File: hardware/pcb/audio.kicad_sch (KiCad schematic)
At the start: 10 parts, among them IC3 TAC5212, J6 PJ-342, J7 PJ-242

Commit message: mainboard: reannotated schematic
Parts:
- renumbered C41 to C111, C47 to C112, C45 to C113, C46 to C114, J6 to J4, J7 to J5, R28 to R32, R26 to R33, R27 to R34
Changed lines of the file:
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@@
 		(in_pos_files yes)
 		(dnp no)
-		(property "Reference" "#PWR087"
+		(property "Reference" "#PWR0104"
 			(at 58.42 33.02 0)
 			(hide yes)
@@
 			(project "meko"
 				(path "/da54f10a-146b-4941-a9c7-55c7173bb101/073f6085-34ed-486a-9dc9-0ac1ede2fab6"
-					(reference "#PWR087")
+					(reference "#PWR0104")
 					(unit 1)
 				)
@@
 		(in_pos_files yes)
 		(dnp no)
-		(property "Reference" "C45"
+		(property "Reference" "C113"
 			(at 52.578 29.464 90)
 			(show_name no)
@@
 			(project "meko"
 				(path "/da54f10a-146b-4941-a9c7-55c7173bb101/073f6085-34ed-486a-9dc9-0ac1ede2fab6"
-					(reference "C45")
+					(reference "C113")
 					(unit 1)
 				)
@@
 		(in_pos_files yes)
 		(dnp no)
-		(property "Reference" "C41"
+		(property "Reference" "C111"
 			(at 62.738 20.574 90)
 			(show_name no)
@@
 			(project "meko"
 				(path "/da54f10a-146b-4941-a9c7-55c7173bb101/073f6085-34ed-486a-9dc9-0ac1ede2fab6"
-					(reference "C41")
+					(reference "C111")
 					(unit 1)
 				)
@@
 		(dnp no)
 		(fields_autoplaced yes)
-		(property "Reference" "#PWR095"
+		(property "Reference" "#PWR0111"
 			(at 44.45 82.55 0)
 			(hide yes)
@@
 			(project "meko"
 				(path "/da54f10a-146b-4941-a9c7-55c7173bb101/073f6085-34ed-486a-9dc9-0ac1ede2fab6"
-					(reference "#PWR095")
+					(reference "#PWR0111")
 					(unit 1)
 				)
@@
 		(in_pos_files yes)
 		(dnp no)
-		(property "Reference" "#PWR0119"
+		(property "Reference" "#PWR0108"
 			(at 97.79 38.1 0)
 			(hide yes)
@@
 			(project "meko"
 				(path "/da54f10a-146b-4941-a9c7-55c7173bb101/073f6085-34ed-486a-9dc9-0ac1ede2fab6"
-					(reference "#PWR0119")
+					(reference "#PWR0108")
 					(unit 1)
 				)
@@
 		(in_pos_files yes)
 		(dnp no)
-		(property "Reference" "R27"
+		(property "Reference" "R34"
 			(at 151.638 93.218 0)
 			(show_name no)
@@
 			(project "meko"
 				(path "/da54f10a-146b-4941-a9c7-55c7173bb101/073f6085-34ed-486a-9dc9-0ac1ede2fab6"
-					(reference "R27")
+					(reference "R34")
 					(unit 1)
 				)
@@
 		(in_pos_files yes)
 		(dnp no)
-		(property "Reference" "#PWR094"
+		(property "Reference" "#PWR0105"
 			(at 88.9 33.02 0)
 			(hide yes)
@@
 			(project "meko"
 				(path "/da54f10a-146b-4941-a9c7-55c7173bb101/073f6085-34ed-486a-9dc9-0ac1ede2fab6"
-					(reference "#PWR094")
+					(reference "#PWR0105")
 					(unit 1)
 				)
@@
 		(in_pos_files yes)
 		(dnp no)
-		(property "Reference" "R26"
+		(property "Reference" "R33"
 			(at 151.638 65.278 0)
 			(show_name no)
@@
 			(project "meko"
 				(path "/da54f10a-146b-4941-a9c7-55c7173bb101/073f6085-34ed-486a-9dc9-0ac1ede2fab6"
-					(reference "R26")
+					(reference "R33")
 					(unit 1)
 				)
@@
 		(in_pos_files yes)
 		(dnp no)
-		(property "Reference" "#PWR0118"
+		(property "Reference" "#PWR0107"
 			(at 49.53 38.1 0)
 			(hide yes)
@@
 			(project "meko"
 				(path "/da54f10a-146b-4941-a9c7-55c7173bb101/073f6085-34ed-486a-9dc9-0ac1ede2fab6"
-					(reference "#PWR0118")
+					(reference "#PWR0107")
 					(unit 1)
 				)
@@
 		(in_pos_files yes)
 		(dnp no)
-		(property "Reference" "#PWR098"
+		(property "Reference" "#PWR0110"
 			(at 154.94 76.2 0)
 			(hide yes)
@@
 			(project "meko"
 				(path "/da54f10a-146b-4941-a9c7-55c7173bb101/073f6085-34ed-486a-9dc9-0ac1ede2fab6"
-					(reference "#PWR098")
+					(reference "#PWR0110")
 					(unit 1)
 				)
@@
 		(in_pos_files yes)
 		(dnp no)
-		(property "Reference" "#PWR090"
+		(property "Reference" "#PWR0103"
 			(at 53.34 21.59 0)
 			(hide yes)
@@
 			(project "meko"
 				(path "/da54f10a-146b-4941-a9c7-55c7173bb101/073f6085-34ed-486a-9dc9-0ac1ede2fab6"
-					(reference "#PWR090")
+					(reference "#PWR0103")
 					(unit 1)
 				)
@@
 		(in_pos_files yes)
 		(dnp no)
-		(property "Reference" "#PWR089"
+		(property "Reference" "#PWR0106"
 			(at 72.39 36.83 0)
 			(hide yes)
@@
 			(project "meko"
 				(path "/da54f10a-146b-4941-a9c7-55c7173bb101/073f6085-34ed-486a-9dc9-0ac1ede2fab6"
-					(reference "#PWR089")
+					(reference "#PWR0106")
 					(unit 1)
 				)
@@
 		(in_pos_files yes)
 		(dnp no)
-		(property "Reference" "C47"
+		(property "Reference" "C112"
 			(at 75.438 28.194 90)
 			(show_name no)
@@
 			(project "meko"
 				(path "/da54f10a-146b-4941-a9c7-55c7173bb101/073f6085-34ed-486a-9dc9-0ac1ede2fab6"
-					(reference "C47")
+					(reference "C112")
 					(unit 1)
 				)
@@
 		(dnp no)
 		(fields_autoplaced yes)
-		(property "Reference" "J7"
+		(property "Reference" "J5"
 			(at 171.45 83.1849 0)
 			(show_name no)
@@
 			(project "meko"
 				(path "/da54f10a-146b-4941-a9c7-55c7173bb101/073f6085-34ed-486a-9dc9-0ac1ede2fab6"
-					(reference "J7")
+					(reference "J5")
 					(unit 1)
 				)
@@
 		(dnp no)
 		(fields_autoplaced yes)
-		(property "Reference" "J6"
+		(property "Reference" "J4"
 			(at 171.45 55.2449 0)
 			(show_name no)
@@
 			(project "meko"
 				(path "/da54f10a-146b-4941-a9c7-55c7173bb101/073f6085-34ed-486a-9dc9-0ac1ede2fab6"
-					(reference "J6")
+					(reference "J4")
 					(unit 1)
 				)
@@
 		(in_pos_files yes)
 		(dnp no)
-		(property "Reference" "#PWR0100"
+		(property "Reference" "#PWR0109"
 			(at 109.22 46.99 0)
 			(hide yes)
@@
 			(project "meko"
 				(path "/da54f10a-146b-4941-a9c7-55c7173bb101/073f6085-34ed-486a-9dc9-0ac1ede2fab6"
-					(reference "#PWR0100")
+					(reference "#PWR0109")
 					(unit 1)
 				)
@@
 		(in_pos_files yes)
 		(dnp no)
-		(property "Reference" "C46"
+		(property "Reference" "C114"
 			(at 94.742 29.464 90)
 			(show_name no)
@@
 			(project "meko"
 				(path "/da54f10a-146b-4941-a9c7-55c7173bb101/073f6085-34ed-486a-9dc9-0ac1ede2fab6"
-					(reference "C46")
+					(reference "C114")
 					(unit 1)
 				)
@@
 		(dnp no)
 		(fields_autoplaced yes)
-		(property "Reference" "#PWR086"
+		(property "Reference" "#PWR0112"
 			(at 73.66 90.17 0)
 			(hide yes)
@@
 			(project "meko"
 				(path "/da54f10a-146b-4941-a9c7-55c7173bb101/073f6085-34ed-486a-9dc9-0ac1ede2fab6"
-					(reference "#PWR086")
+					(reference "#PWR0112")
 					(unit 1)
 				)
@@
 		(in_pos_files yes)
 		(dnp no)
-		(property "Reference" "R28"
+		(property "Reference" "R32"
 			(at 117.602 46.228 0)
 			(show_name no)
@@
 			(project "meko"
 				(path "/da54f10a-146b-4941-a9c7-55c7173bb101/073f6085-34ed-486a-9dc9-0ac1ede2fab6"
-					(reference "R28")
+					(reference "R32")
 					(unit 1)
 				)
@@
 		(in_pos_files yes)
 		(dnp no)
-		(property "Reference" "#PWR099"
+		(property "Reference" "#PWR0113"
 			(at 154.94 104.14 0)
 			(hide yes)
@@
 			(project "meko"
 				(path "/da54f10a-146b-4941-a9c7-55c7173bb101/073f6085-34ed-486a-9dc9-0ac1ede2fab6"
-					(reference "#PWR099")
-					(unit 1)
-				)
+					(reference "#PWR0113")
+					(unit 1)
+				)

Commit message: added a bunch testpoints
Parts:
- added TP52: AU_BCLK, TestPoint:TestPoint_Pad_D1.0mm, symbol Connector:TestPoint
- added TP53: AU_FSYNC, TestPoint:TestPoint_Pad_D1.0mm, symbol Connector:TestPoint
- added TP54: AU_DOUT, TestPoint:TestPoint_Pad_D1.0mm, symbol Connector:TestPoint
- added TP55: AU_DIN, TestPoint:TestPoint_Pad_D1.0mm, symbol Connector:TestPoint
- added TP56: AU_GPIO1, TestPoint:TestPoint_Pad_D1.0mm, symbol Connector:TestPoint
- added TP57: AU_GPIO2, TestPoint:TestPoint_Pad_D1.0mm, symbol Connector:TestPoint
- added TP58: AU_GPO1, TestPoint:TestPoint_Pad_D1.0mm, symbol Connector:TestPoint
- added TP59: AU_GPI1, TestPoint:TestPoint_Pad_D1.0mm, symbol Connector:TestPoint
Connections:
- net BCLK: now also TP52.1
- net DIN: now also TP55.1
- net DOUT: now also TP54.1
- net FSYNC: now also TP53.1
- net GPI1: now also TP59.1
- net GPIO1: now also TP56.1
- net GPIO2: now also TP57.1
- net GPO1: now also TP58.1

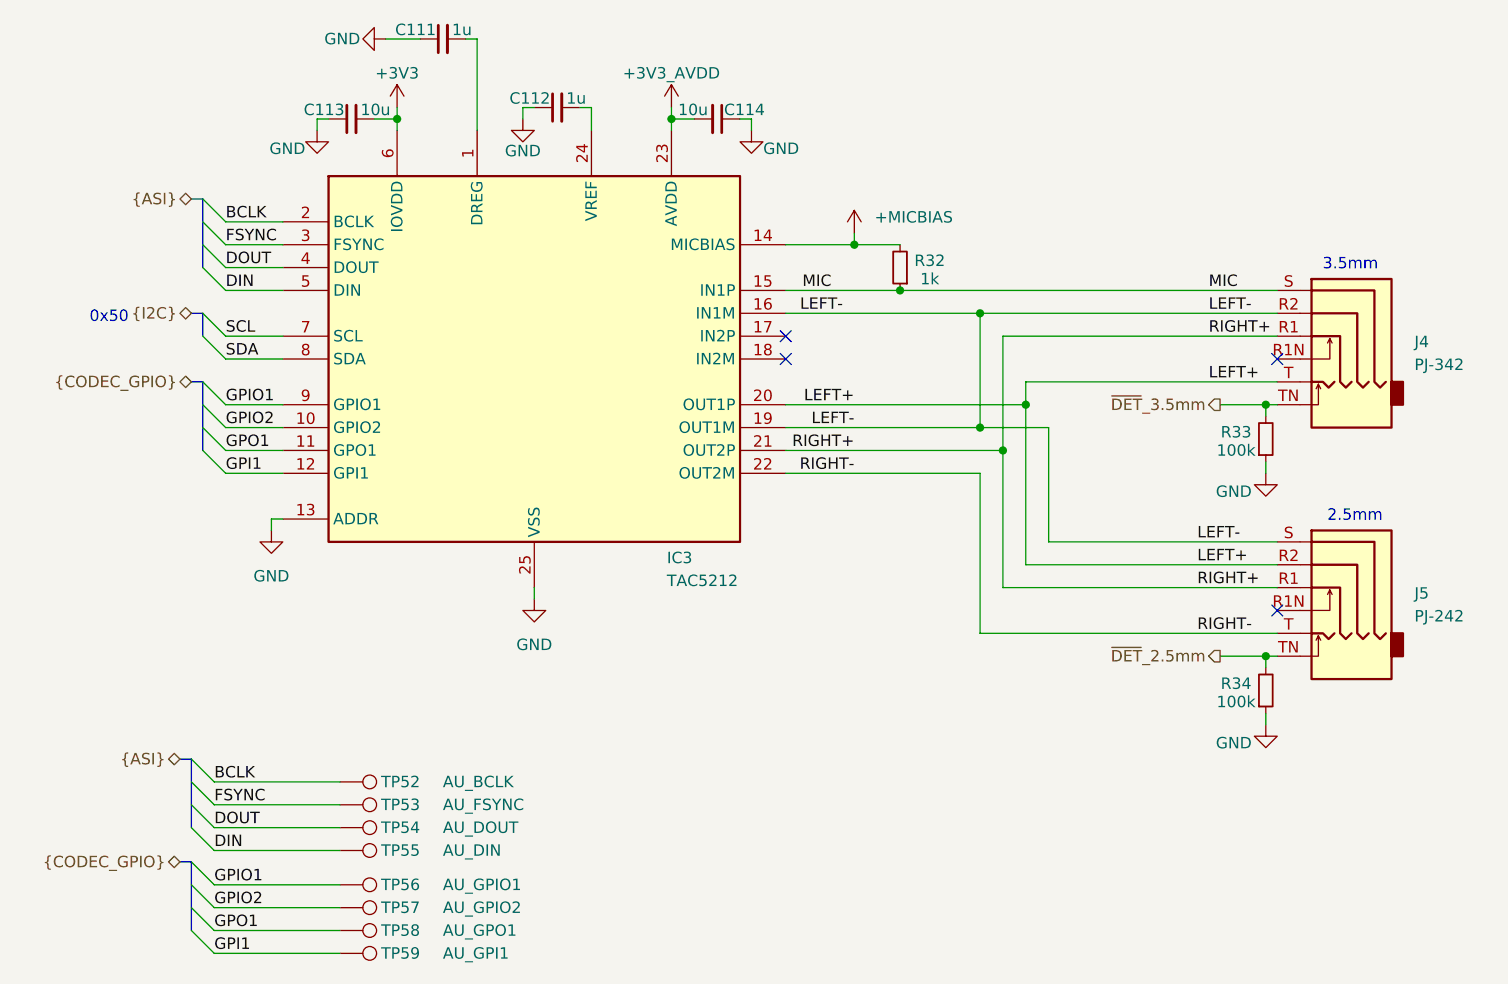
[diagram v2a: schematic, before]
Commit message: removed testpoints on sd cards, since I can probe the pins there
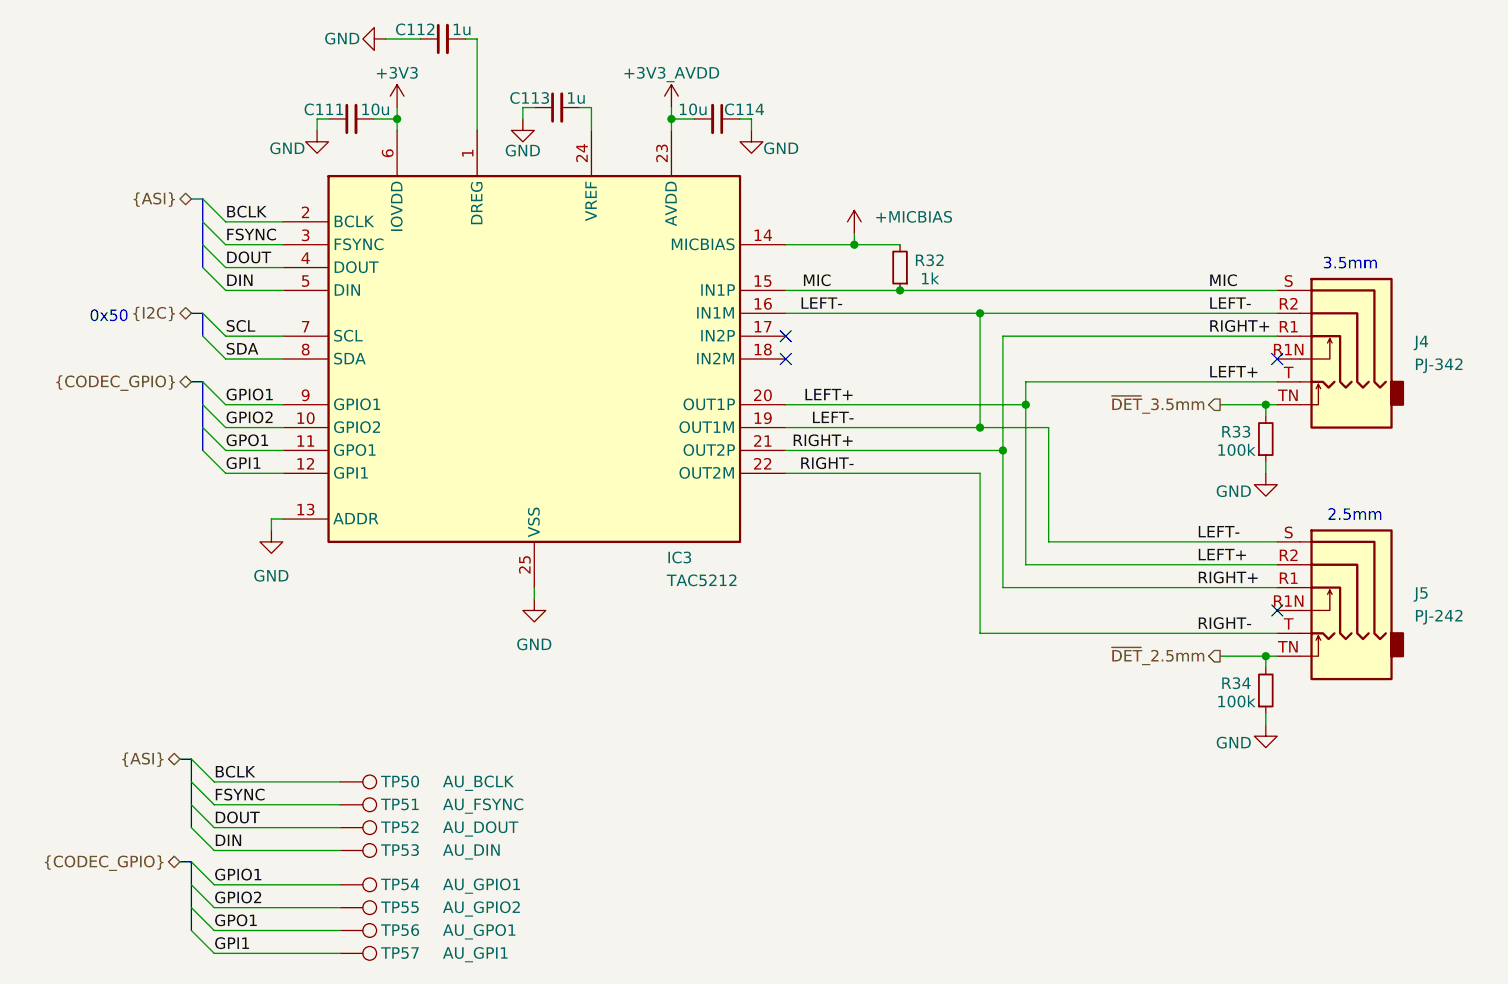
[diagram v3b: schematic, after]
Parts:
- renumbered C113 to C111, C111 to C112, C112 to C113, TP52 to TP50, TP53 to TP51, TP54 to TP52, TP55 to TP53, TP56 to TP54, TP57 to TP55, TP58 to TP56, TP59 to TP57
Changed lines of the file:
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@@
 		(in_pos_files yes)
 		(dnp no)
-		(property "Reference" "#PWR0104"
+		(property "Reference" "#PWR0106"
 			(at 58.42 33.02 0)
 			(hide yes)
@@
 			(project "meko"
 				(path "/da54f10a-146b-4941-a9c7-55c7173bb101/073f6085-34ed-486a-9dc9-0ac1ede2fab6"
-					(reference "#PWR0104")
+					(reference "#PWR0106")
 					(unit 1)
 				)
@@
 		(in_pos_files yes)
 		(dnp no)
-		(property "Reference" "C113"
+		(property "Reference" "C111"
 			(at 52.578 29.464 90)
 			(show_name no)
@@
 			(project "meko"
 				(path "/da54f10a-146b-4941-a9c7-55c7173bb101/073f6085-34ed-486a-9dc9-0ac1ede2fab6"
-					(reference "C113")
+					(reference "C111")
 					(unit 1)
 				)
@@
 		(in_pos_files yes)
 		(dnp no)
-		(property "Reference" "C111"
+		(property "Reference" "C112"
 			(at 62.738 20.574 90)
 			(show_name no)
@@
 			(project "meko"
 				(path "/da54f10a-146b-4941-a9c7-55c7173bb101/073f6085-34ed-486a-9dc9-0ac1ede2fab6"
-					(reference "C111")
+					(reference "C112")
 					(unit 1)
 				)
@@
 		(in_pos_files yes)
 		(dnp no)
-		(property "Reference" "TP52"
+		(property "Reference" "TP50"
 			(at 56.642 104.14 90)
 			(show_name no)
@@
 			(project "meko"
 				(path "/da54f10a-146b-4941-a9c7-55c7173bb101/073f6085-34ed-486a-9dc9-0ac1ede2fab6"
-					(reference "TP52")
+					(reference "TP50")
 					(unit 1)
 				)
@@
 		(in_pos_files yes)
 		(dnp no)
-		(property "Reference" "TP56"
+		(property "Reference" "TP54"
 			(at 56.642 115.57 90)
 			(show_name no)
@@
 			(project "meko"
 				(path "/da54f10a-146b-4941-a9c7-55c7173bb101/073f6085-34ed-486a-9dc9-0ac1ede2fab6"
-					(reference "TP56")
+					(reference "TP54")
 					(unit 1)
 				)
@@
 		(dnp no)
 		(fields_autoplaced yes)
-		(property "Reference" "#PWR0111"
+		(property "Reference" "#PWR0103"
 			(at 44.45 82.55 0)
 			(hide yes)
@@
 			(project "meko"
 				(path "/da54f10a-146b-4941-a9c7-55c7173bb101/073f6085-34ed-486a-9dc9-0ac1ede2fab6"
-					(reference "#PWR0111")
+					(reference "#PWR0103")
 					(unit 1)
 				)
@@
 		(in_pos_files yes)
 		(dnp no)
-		(property "Reference" "TP54"
+		(property "Reference" "TP52"
 			(at 56.642 109.22 90)
 			(show_name no)
@@
 			(project "meko"
 				(path "/da54f10a-146b-4941-a9c7-55c7173bb101/073f6085-34ed-486a-9dc9-0ac1ede2fab6"
-					(reference "TP54")
+					(reference "TP52")
 					(unit 1)
 				)
@@
 		(in_pos_files yes)
 		(dnp no)
-		(property "Reference" "#PWR0108"
+		(property "Reference" "#PWR0110"
 			(at 97.79 38.1 0)
 			(hide yes)
@@
 			(project "meko"
 				(path "/da54f10a-146b-4941-a9c7-55c7173bb101/073f6085-34ed-486a-9dc9-0ac1ede2fab6"
-					(reference "#PWR0108")
+					(reference "#PWR0110")
 					(unit 1)
 				)
@@
 		(in_pos_files yes)
 		(dnp no)
-		(property "Reference" "TP53"
+		(property "Reference" "TP51"
 			(at 56.642 106.68 90)
 			(show_name no)
@@
 			(project "meko"
 				(path "/da54f10a-146b-4941-a9c7-55c7173bb101/073f6085-34ed-486a-9dc9-0ac1ede2fab6"
-					(reference "TP53")
+					(reference "TP51")
 					(unit 1)
 				)
@@
 		(in_pos_files yes)
 		(dnp no)
-		(property "Reference" "TP57"
+		(property "Reference" "TP55"
 			(at 56.642 118.11 90)
 			(show_name no)
@@
 			(project "meko"
 				(path "/da54f10a-146b-4941-a9c7-55c7173bb101/073f6085-34ed-486a-9dc9-0ac1ede2fab6"
-					(reference "TP57")
+					(reference "TP55")
 					(unit 1)
 				)
@@
 		(in_pos_files yes)
 		(dnp no)
-		(property "Reference" "#PWR0105"
+		(property "Reference" "#PWR0109"
 			(at 88.9 33.02 0)
 			(hide yes)
@@
 			(project "meko"
 				(path "/da54f10a-146b-4941-a9c7-55c7173bb101/073f6085-34ed-486a-9dc9-0ac1ede2fab6"
-					(reference "#PWR0105")
+					(reference "#PWR0109")
 					(unit 1)
 				)
@@
 		(in_pos_files yes)
 		(dnp no)
-		(property "Reference" "#PWR0107"
+		(property "Reference" "#PWR0104"
 			(at 49.53 38.1 0)
 			(hide yes)
@@
 			(project "meko"
 				(path "/da54f10a-146b-4941-a9c7-55c7173bb101/073f6085-34ed-486a-9dc9-0ac1ede2fab6"
-					(reference "#PWR0107")
+					(reference "#PWR0104")
 					(unit 1)
 				)
@@
 		(in_pos_files yes)
 		(dnp no)
-		(property "Reference" "#PWR0110"
+		(property "Reference" "#PWR0112"
 			(at 154.94 76.2 0)
 			(hide yes)
@@
 			(project "meko"
 				(path "/da54f10a-146b-4941-a9c7-55c7173bb101/073f6085-34ed-486a-9dc9-0ac1ede2fab6"
-					(reference "#PWR0110")
+					(reference "#PWR0112")
 					(unit 1)
 				)
@@
 		(in_pos_files yes)
 		(dnp no)
-		(property "Reference" "TP59"
+		(property "Reference" "TP57"
 			(at 56.642 123.19 90)
 			(show_name no)
@@
 			(project "meko"
 				(path "/da54f10a-146b-4941-a9c7-55c7173bb101/073f6085-34ed-486a-9dc9-0ac1ede2fab6"
-					(reference "TP59")
+					(reference "TP57")
 					(unit 1)
 				)
@@
 		(in_pos_files yes)
 		(dnp no)
-		(property "Reference" "#PWR0103"
+		(property "Reference" "#PWR0105"
 			(at 50.8 21.59 0)
 			(hide yes)
@@
 			(project "meko"
 				(path "/da54f10a-146b-4941-a9c7-55c7173bb101/073f6085-34ed-486a-9dc9-0ac1ede2fab6"
-					(reference "#PWR0103")
+					(reference "#PWR0105")
 					(unit 1)
 				)
@@
 		(in_pos_files yes)
 		(dnp no)
-		(property "Reference" "#PWR0106"
+		(property "Reference" "#PWR0107"
 			(at 72.39 36.83 0)
 			(hide yes)
@@
 			(project "meko"
 				(path "/da54f10a-146b-4941-a9c7-55c7173bb101/073f6085-34ed-486a-9dc9-0ac1ede2fab6"
-					(reference "#PWR0106")
+					(reference "#PWR0107")
 					(unit 1)
 				)
@@
 		(in_pos_files yes)
 		(dnp no)
-		(property "Reference" "C112"
+		(property "Reference" "C113"
 			(at 75.438 28.194 90)
 			(show_name no)
@@
 			(project "meko"
 				(path "/da54f10a-146b-4941-a9c7-55c7173bb101/073f6085-34ed-486a-9dc9-0ac1ede2fab6"
-					(reference "C112")
+					(reference "C113")
 					(unit 1)
 				)
@@
 		(in_pos_files yes)
 		(dnp no)
-		(property "Reference" "TP55"
+		(property "Reference" "TP53"
 			(at 56.642 111.76 90)
 			(show_name no)
@@
 			(project "meko"
 				(path "/da54f10a-146b-4941-a9c7-55c7173bb101/073f6085-34ed-486a-9dc9-0ac1ede2fab6"
-					(reference "TP55")
+					(reference "TP53")
 					(unit 1)
 				)
@@
 		(in_pos_files yes)
 		(dnp no)
-		(property "Reference" "#PWR0109"
+		(property "Reference" "#PWR0111"
 			(at 109.22 46.99 0)
 			(hide yes)
@@
 			(project "meko"
 				(path "/da54f10a-146b-4941-a9c7-55c7173bb101/073f6085-34ed-486a-9dc9-0ac1ede2fab6"
-					(reference "#PWR0109")
+					(reference "#PWR0111")
 					(unit 1)
 				)
@@
 		(dnp no)
 		(fields_autoplaced yes)
-		(property "Reference" "#PWR0112"
+		(property "Reference" "#PWR0108"
 			(at 73.66 90.17 0)
 			(hide yes)
@@
 			(project "meko"
 				(path "/da54f10a-146b-4941-a9c7-55c7173bb101/073f6085-34ed-486a-9dc9-0ac1ede2fab6"
-					(reference "#PWR0112")
+					(reference "#PWR0108")
 					(unit 1)
 				)
@@
 		(in_pos_files yes)
 		(dnp no)
-		(property "Reference" "TP58"
+		(property "Reference" "TP56"
 			(at 56.642 120.65 90)
 			(show_name no)
@@
 			(project "meko"
 				(path "/da54f10a-146b-4941-a9c7-55c7173bb101/073f6085-34ed-486a-9dc9-0ac1ede2fab6"
-					(reference "TP58")
-					(unit 1)
-				)
+					(reference "TP56")
+					(unit 1)
+				)
